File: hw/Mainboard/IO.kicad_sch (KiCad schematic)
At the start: 10 parts, among them U7 W65C21N, U8 W65C21N, U9 W65C22N

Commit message: hw: wip
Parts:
- NT10, NT13, NT14, NT15: symbol Device:NetTie_2 -> PET:PowerTie_2
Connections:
- removed net +5V: C7.1, C8.1, C9.1, NT10.2, NT13.2, NT14.2, U7.22 (CS0), U7.24 (CS1), U8.22 (CS0), U8.24 (CS1), U9.24 (CS1)
- new net: C8.1, NT13.2, U8.22 (CS0), U8.24 (CS1)
- new net: C9.1, NT10.2, U7.22 (CS0), U7.24 (CS1), U9.24 (CS1)
- new net: C7.1, NT14.2
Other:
- moved on the sheet: C7, C8, C9, U7, U8, U9

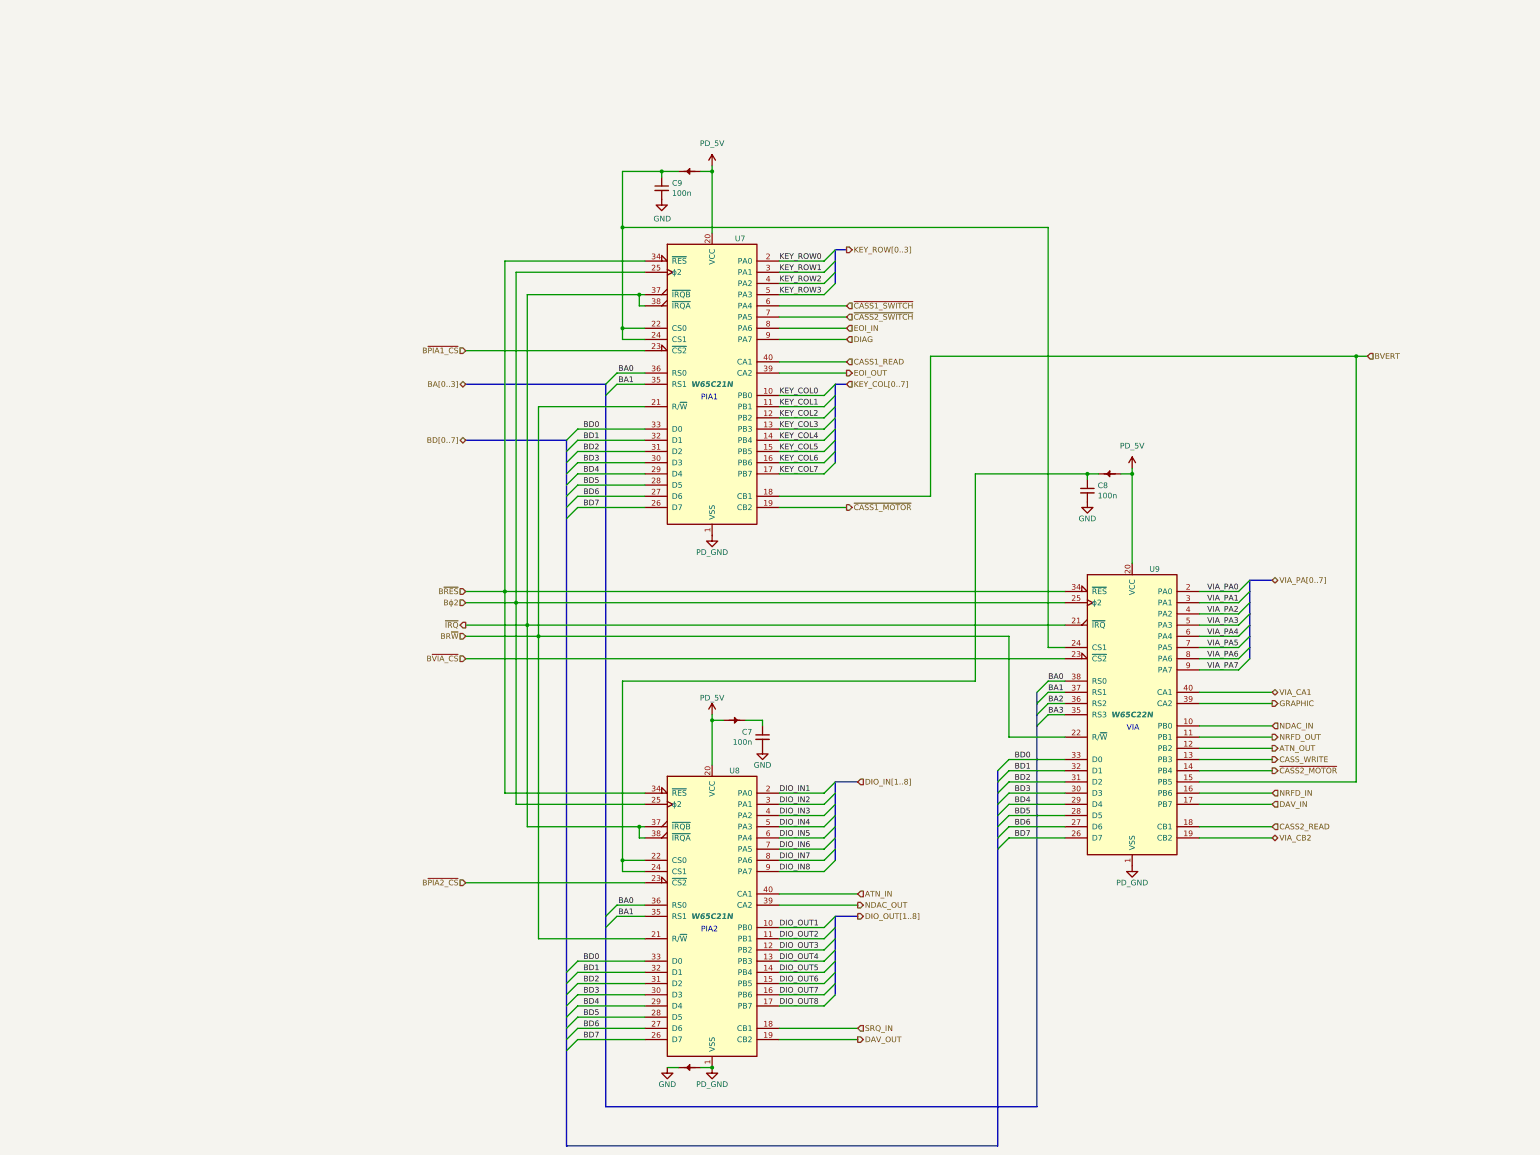
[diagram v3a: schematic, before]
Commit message: hw: tidy power and resize pages
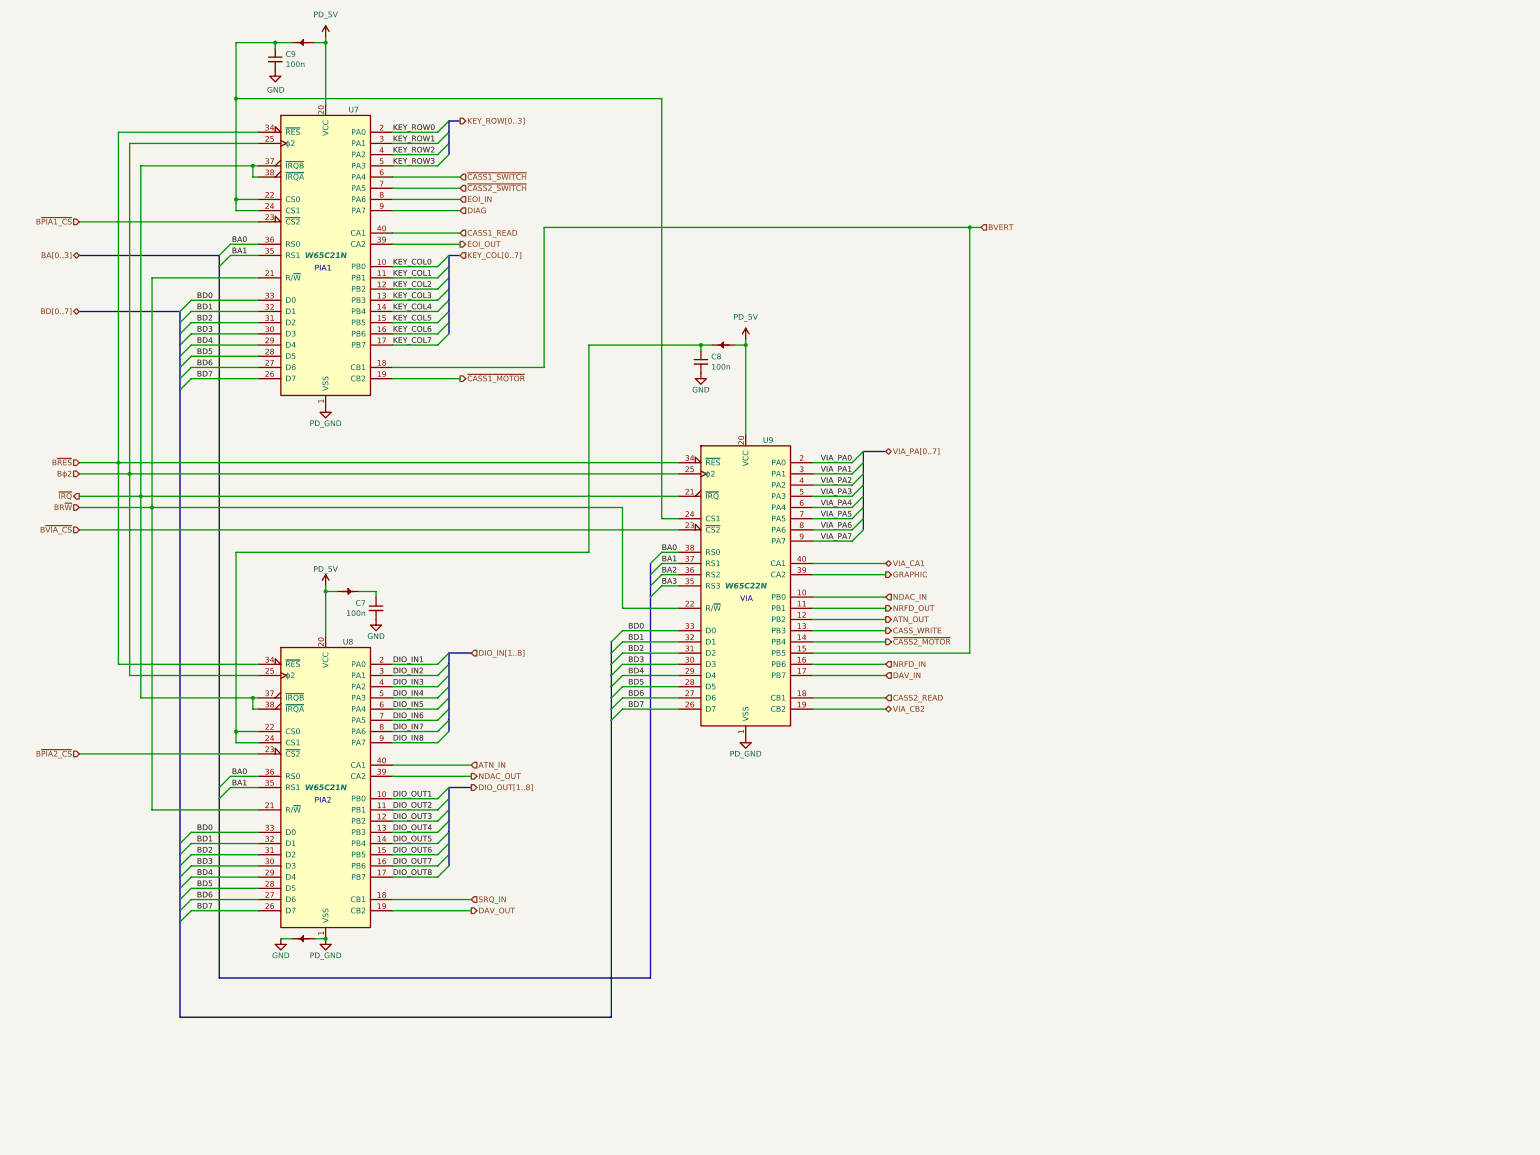
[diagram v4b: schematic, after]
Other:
- title: (none) -> CBM PET Mainboard Replacement
- moved on the sheet: C7, C8, C9, U7, U8, U9

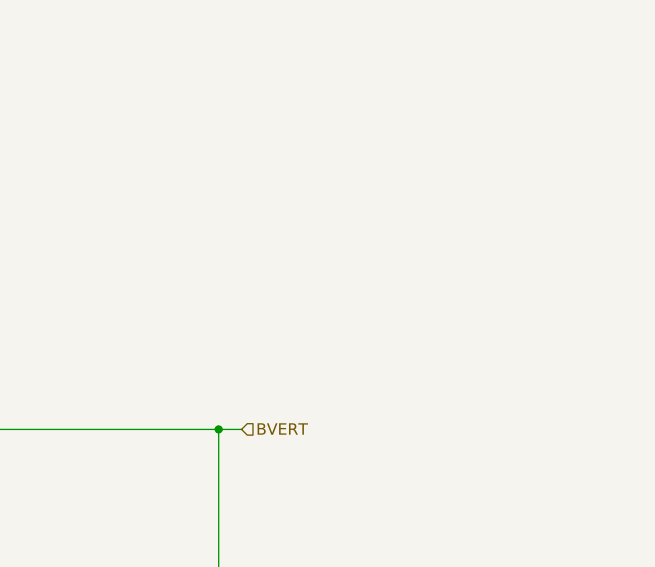
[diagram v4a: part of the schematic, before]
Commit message: hw: tidy CPU, rename RD/WR strobe to RAM_OE/_WE, debounce switches
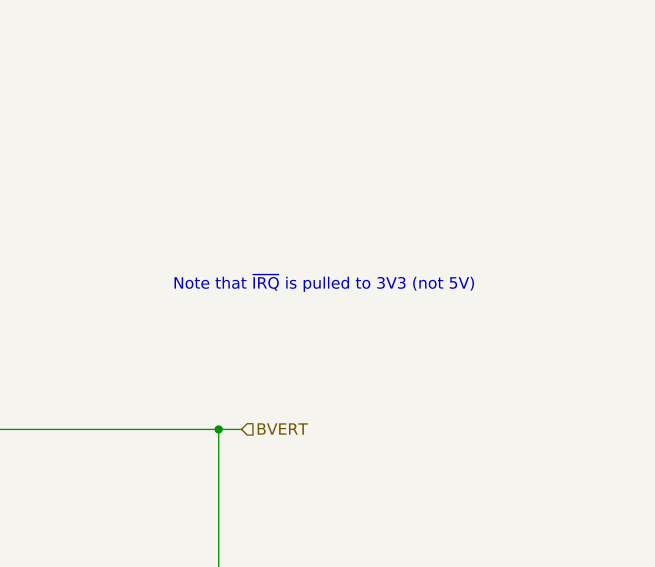
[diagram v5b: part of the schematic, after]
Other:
- note added: "Note that ~{IRQ} is pulled to 3V3 (not 5V)"
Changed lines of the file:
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@@
+    (effects (font (size 1.27 1.27)) (justify left bottom))
+  )
+  (text "Note that ~{IRQ} is pulled to 3V3 (not 5V)" (at 222.25 22.86 0)
     (effects (font (size 1.27 1.27)) (justify left bottom))
   )

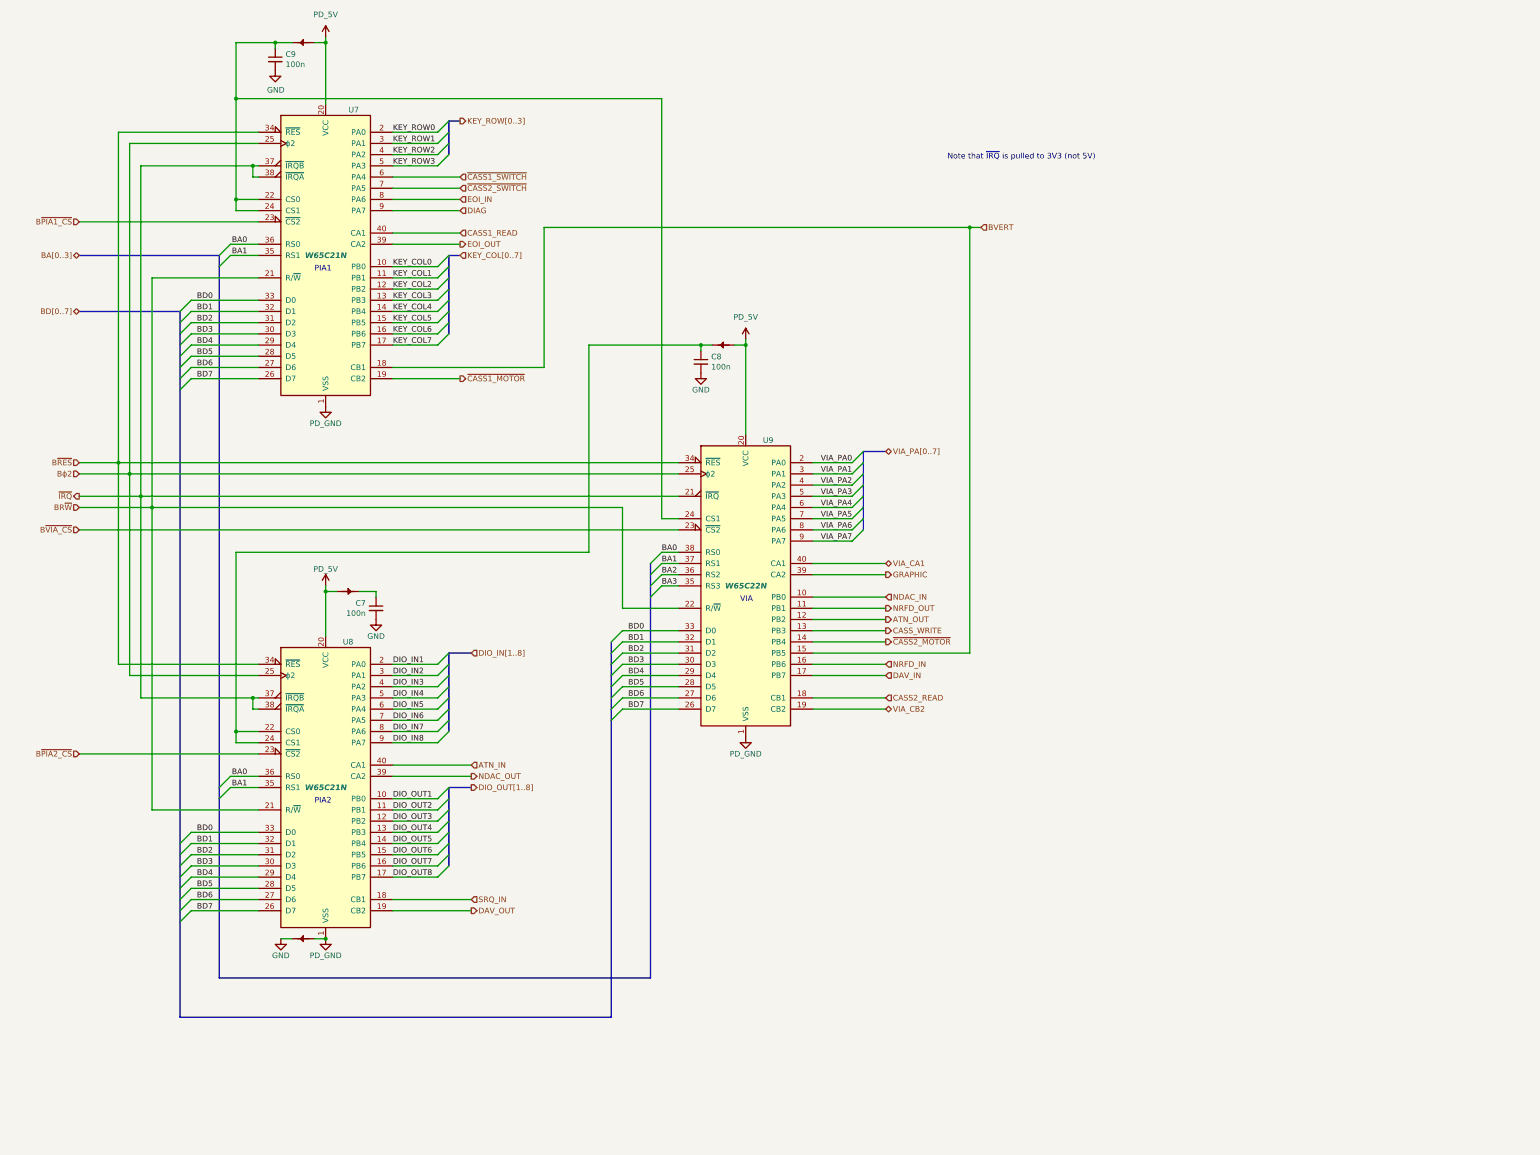
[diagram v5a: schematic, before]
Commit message: hw: tidy IO, move CPU decoupling caps
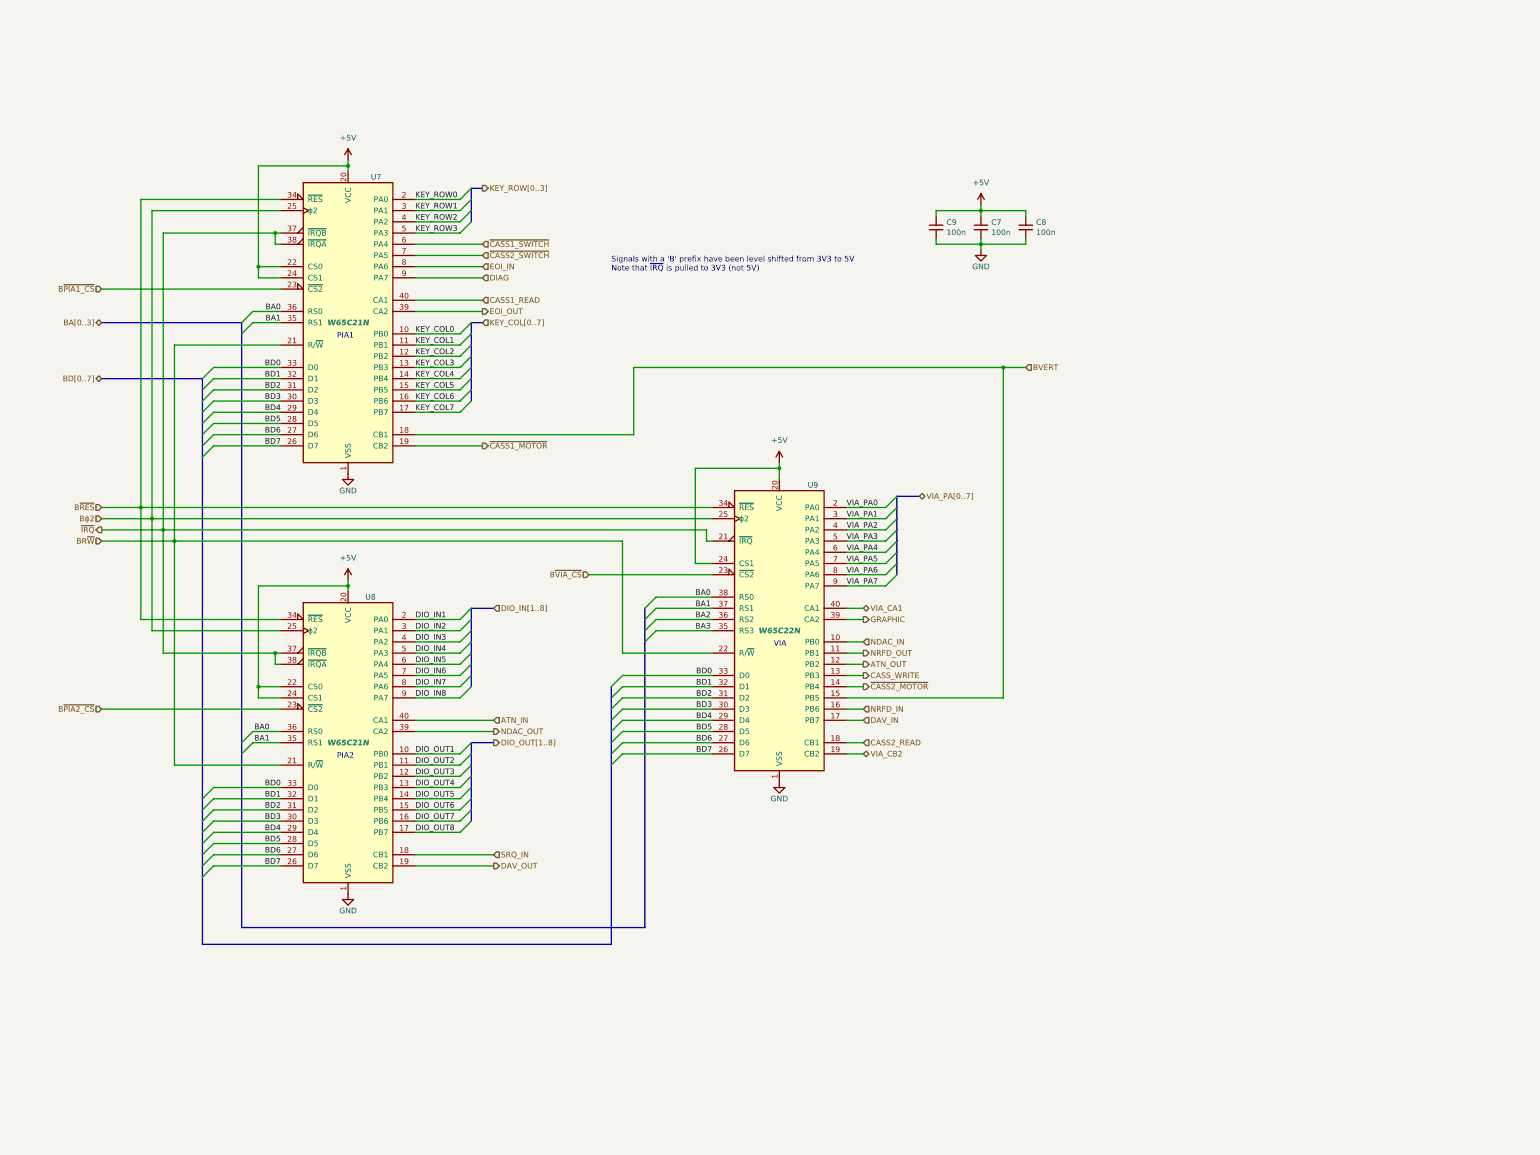
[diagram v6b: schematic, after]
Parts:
- removed NT10, NT13, NT14, NT15: +5V, PET:NetTie-2_SMD_Pad_1.6_to_0.4mm, symbol PET:PowerTie_2
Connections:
- net PD_5V is gone; now on net +5V: U7.20 (VCC), U8.20 (VCC), U9.20 (VCC)
- net PD_GND is gone; now on net GND: U7.1 (VSS), U8.1 (VSS), U9.1 (VSS)
- net +5V: now reaches C8.1, U8.22 (CS0), U8.24 (CS1)
- net +5V: now also C7.1, C9.1, U7.22 (CS0), U7.24 (CS1), U9.24 (CS1)
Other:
- note added: "Signals with a 'B' prefix have been level shifted from 3V3 to 5V Note that ~{IRQ} is pulled to 3V3 (not 5V)"
- note removed: "Note that ~{IRQ} is pulled to 3V3 (not 5V)"
- moved on the sheet: C7, C8, C9, U7, U8, U9

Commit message: hw: tidy audio, cass, IEEE, keyboard, magic, user
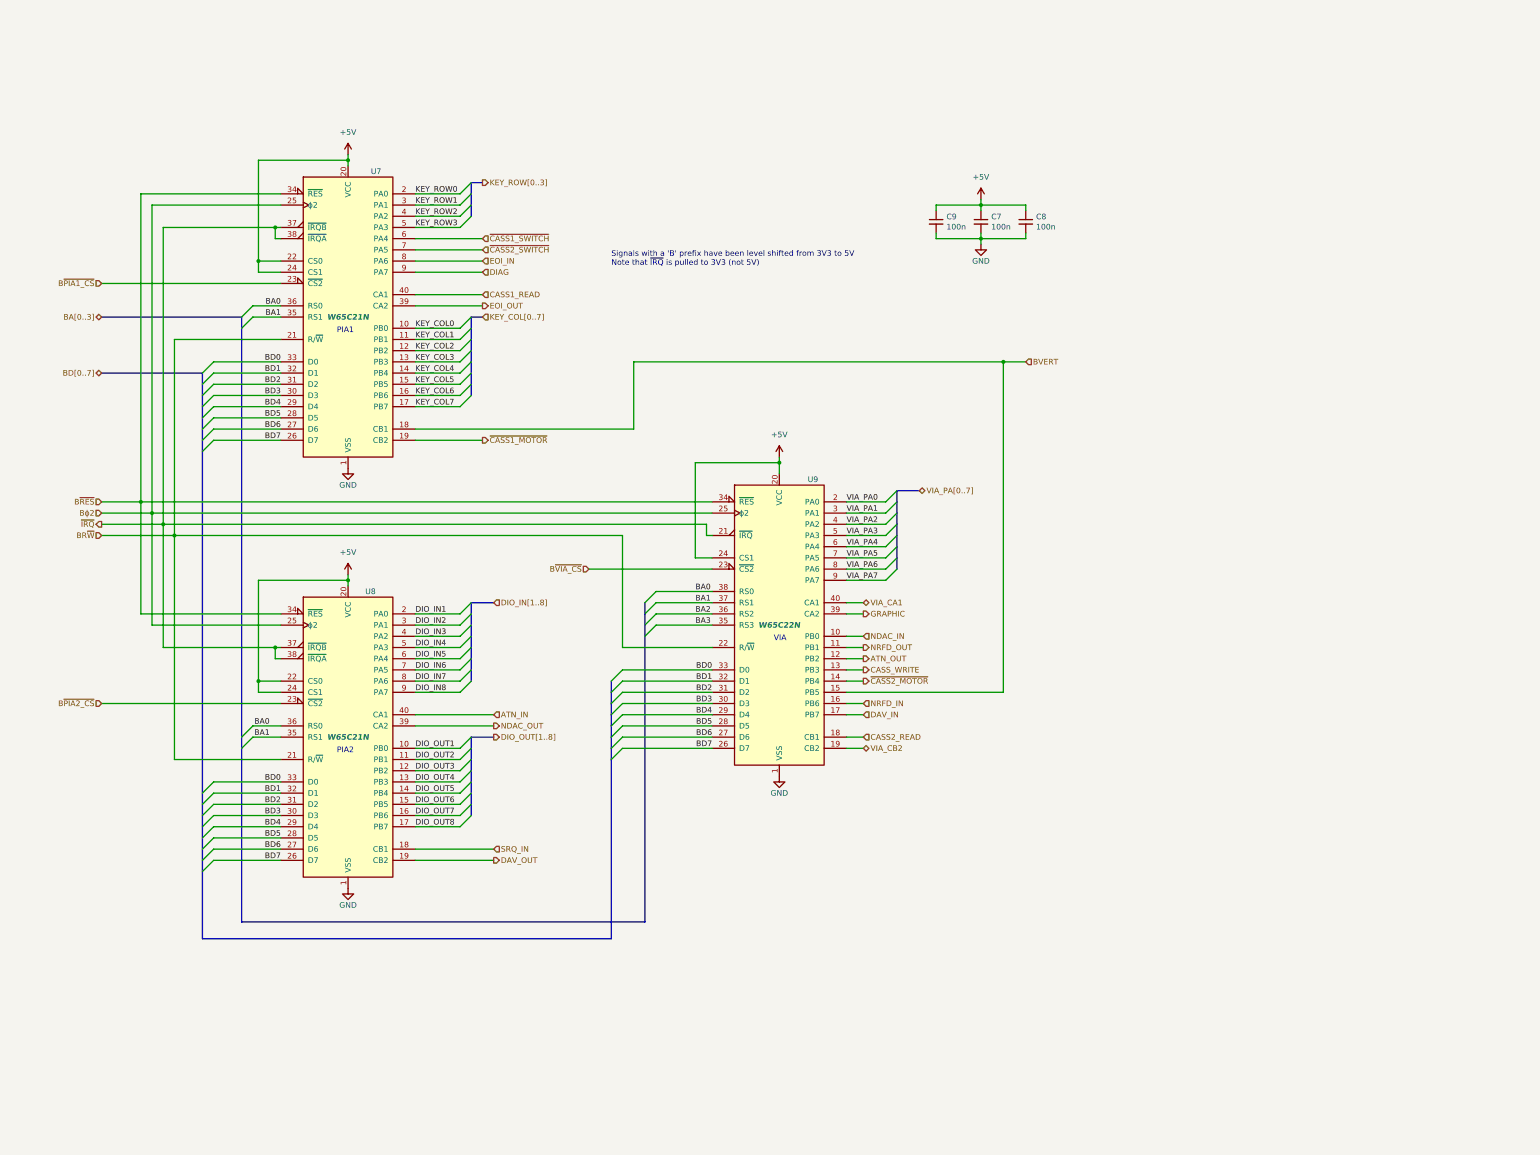
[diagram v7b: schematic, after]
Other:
- moved on the sheet: C7, C8, C9, U7, U8, U9

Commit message: hw: comments
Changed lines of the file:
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@@
     (stroke (width 0) (type default) (color 0 0 0 0))
+  )
+  (text "PIA1" (at 66.04 21.59 0)
+    (effects (font (size 1.5 1.5) (thickness 0.8) bold) (justify left bottom))
   )
   (text "PIA2" (at 83.82 157.48 0)
     (effects (font (size 1.27 1.27)) (justify left bottom))
   )
-  (text "PIA1" (at 83.82 62.23 0)
-    (effects (font (size 1.27 1.27)) (justify left bottom))
+  (text "PIA2" (at 66.04 116.84 0)
+    (effects (font (size 1.5 1.5) (thickness 0.8) bold) (justify left bottom))
   )
   (text "VIA" (at 182.88 132.08 0)
@@
     (effects (font (size 1.27 1.27)) (justify left bottom))
   )
+  (text "VIA" (at 165.1 90.17 0)
+    (effects (font (size 1.5 1.5) (thickness 0.8) bold) (justify left bottom))
+  )
   (label "KEY_COL5" (at 101.6 73.66 0)
